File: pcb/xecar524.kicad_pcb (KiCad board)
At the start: 2 copper layers, 63.8 x 88.9 mm, 40 parts, among them J1 JTAG, J2 PROG, J3 Conn_02x02_Odd_Even, U1 MCP1703A-3302_SOT89, U2 Atari_XE_Cartridge_Connector, U3 XC95144XL-TQ100, U4 SST39VF040

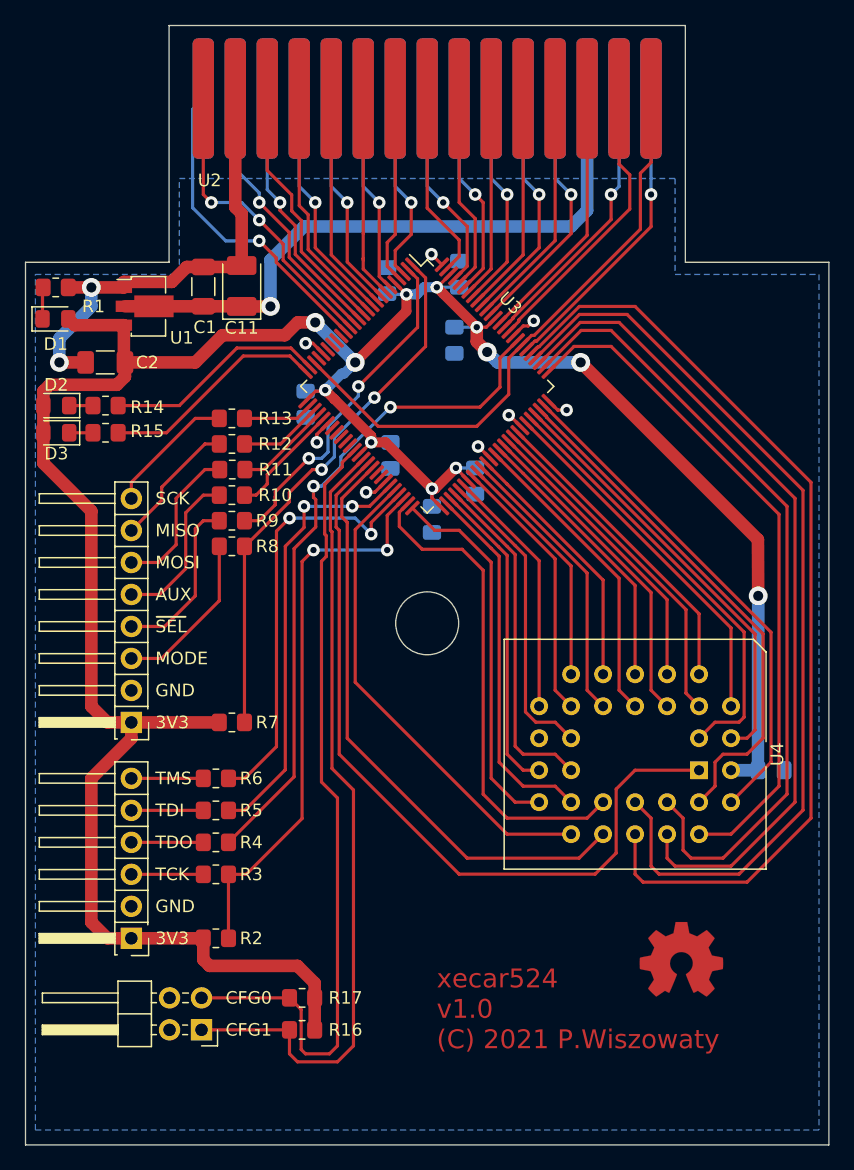
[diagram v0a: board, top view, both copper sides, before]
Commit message: PCB: Add top GND copper pour
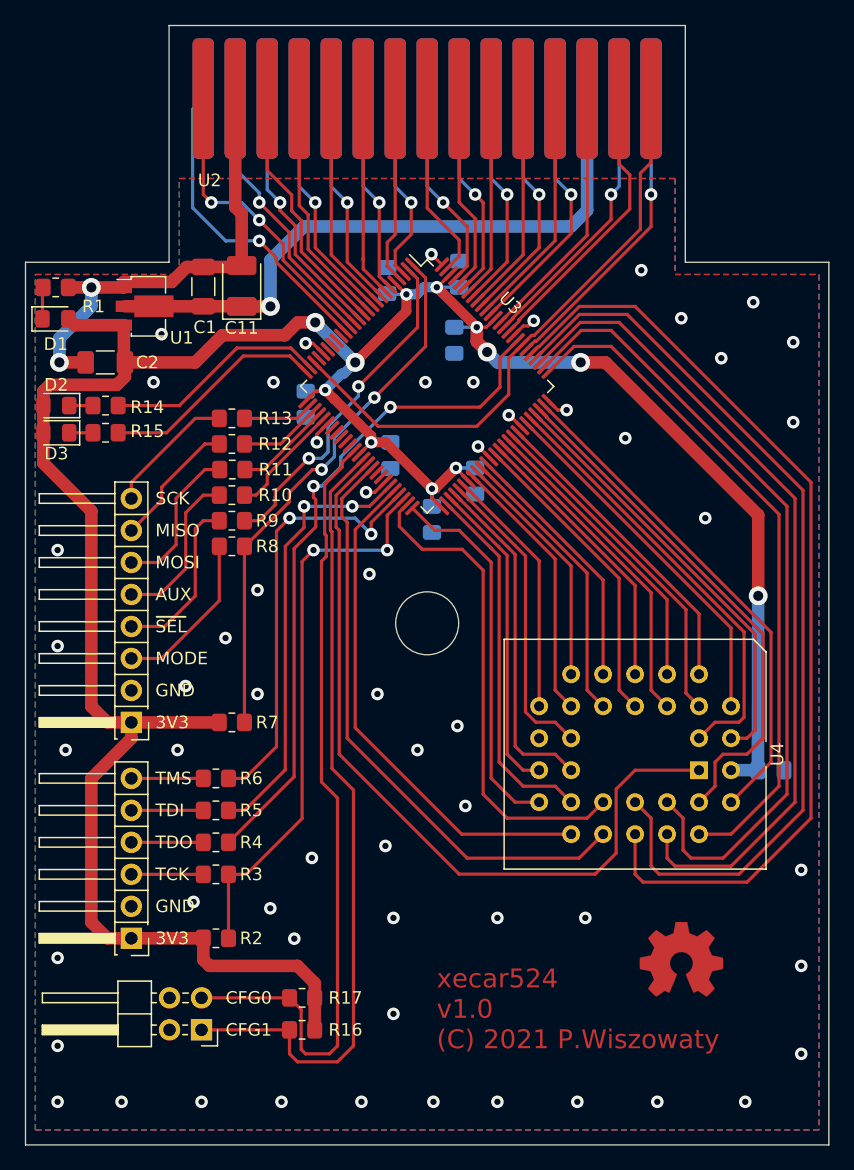
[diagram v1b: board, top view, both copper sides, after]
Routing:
- net ROM_D7: track 38.7 -> 40.8 mm
- net +3V3: track 220.6 -> 221.8 mm
- net GND: vias 10 -> 60
- added copper zone on F.Cu, net GND
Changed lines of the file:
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@@
     (thickness 1.6)
     (drawings 26)
-    (tracks 608)
+    (tracks 659)
     (zones 0)
     (modules 40)
@@
   (segment (start 135.268 59.644) (end 134.76 59.136) (width 1) (layer F.Cu) (net 3))
   (segment (start 135.268 63.76) (end 135.268 59.644) (width 1) (layer F.Cu) (net 3))
+  (via (at 139.446 117.221) (size 1) (drill 0.5) (layers F.Cu B.Cu) (net 3))
+  (via (at 137.541 114.808) (size 1) (drill 0.5) (layers F.Cu B.Cu) (net 3))
+  (via (at 140.843 110.8075) (size 1) (drill 0.5) (layers F.Cu B.Cu) (net 3))
+  (via (at 153.035 106.68) (size 1) (drill 0.5) (layers F.Cu B.Cu) (net 3))
+  (via (at 152.4 100.33) (size 1) (drill 0.5) (layers F.Cu B.Cu) (net 3))
+  (via (at 149.225 102.235) (size 1) (drill 0.5) (layers F.Cu B.Cu) (net 3))
+  (via (at 146.05 97.79) (size 1) (drill 0.5) (layers F.Cu B.Cu) (net 3))
+  (via (at 145.415 88.265) (size 1) (drill 0.5) (layers F.Cu B.Cu) (net 3))
+  (via (at 179.07 76.2) (size 1) (drill 0.5) (layers F.Cu B.Cu) (net 3))
+  (via (at 179.07 69.85) (size 1) (drill 0.5) (layers F.Cu B.Cu) (net 3))
+  (via (at 175.895 66.675) (size 1) (drill 0.5) (layers F.Cu B.Cu) (net 3))
+  (via (at 173.355 71.12) (size 1) (drill 0.5) (layers F.Cu B.Cu) (net 3))
+  (via (at 170.18 67.945) (size 1) (drill 0.5) (layers F.Cu B.Cu) (net 3))
+  (via (at 167.005 64.135) (size 1) (drill 0.5) (layers F.Cu B.Cu) (net 3))
+  (via (at 149.86 73.025) (size 1) (drill 0.5) (layers F.Cu B.Cu) (net 3))
+  (via (at 153.67 73.025) (size 1) (drill 0.5) (layers F.Cu B.Cu) (net 3))
+  (via (at 137.795 73.025) (size 1) (drill 0.5) (layers F.Cu B.Cu) (net 3))
+  (via (at 128.27 73.025) (size 1) (drill 0.5) (layers F.Cu B.Cu) (net 3))
+  (via (at 128.905 69.215) (size 1) (drill 0.5) (layers F.Cu B.Cu) (net 3))
+  (via (at 130.175 102.235) (size 1) (drill 0.5) (layers F.Cu B.Cu) (net 3))
+  (via (at 136.525 97.79) (size 1) (drill 0.5) (layers F.Cu B.Cu) (net 3))
+  (via (at 136.525 89.535) (size 1) (drill 0.5) (layers F.Cu B.Cu) (net 3))
+  (via (at 165.735 77.47) (size 1) (drill 0.5) (layers F.Cu B.Cu) (net 3))
+  (via (at 172.085 83.82) (size 1) (drill 0.5) (layers F.Cu B.Cu) (net 3))
+  (via (at 120.65 86.36) (size 1) (drill 0.5) (layers F.Cu B.Cu) (net 3))
+  (via (at 120.65 93.98) (size 1) (drill 0.5) (layers F.Cu B.Cu) (net 3))
+  (via (at 130.81 97.155) (size 1) (drill 0.5) (layers F.Cu B.Cu) (net 3))
+  (via (at 133.985 93.345) (size 1) (drill 0.5) (layers F.Cu B.Cu) (net 3))
+  (via (at 121.285 102.235) (size 1) (drill 0.5) (layers F.Cu B.Cu) (net 3))
+  (via (at 131.445 114.3) (size 1) (drill 0.5) (layers F.Cu B.Cu) (net 3))
+  (via (at 120.65 118.745) (size 1) (drill 0.5) (layers F.Cu B.Cu) (net 3))
+  (via (at 120.65 125.73) (size 1) (drill 0.5) (layers F.Cu B.Cu) (net 3))
+  (via (at 120.65 130.175) (size 1) (drill 0.5) (layers F.Cu B.Cu) (net 3))
+  (via (at 125.73 130.175) (size 1) (drill 0.5) (layers F.Cu B.Cu) (net 3))
+  (via (at 132.08 130.175) (size 1) (drill 0.5) (layers F.Cu B.Cu) (net 3))
+  (via (at 138.43 130.175) (size 1) (drill 0.5) (layers F.Cu B.Cu) (net 3))
+  (via (at 144.78 130.175) (size 1) (drill 0.5) (layers F.Cu B.Cu) (net 3))
+  (via (at 150.495 130.175) (size 1) (drill 0.5) (layers F.Cu B.Cu) (net 3))
+  (via (at 155.575 130.175) (size 1) (drill 0.5) (layers F.Cu B.Cu) (net 3))
+  (via (at 161.925 130.175) (size 1) (drill 0.5) (layers F.Cu B.Cu) (net 3))
+  (via (at 168.275 130.175) (size 1) (drill 0.5) (layers F.Cu B.Cu) (net 3))
+  (via (at 175.26 130.175) (size 1) (drill 0.5) (layers F.Cu B.Cu) (net 3))
+  (via (at 179.705 126.365) (size 1) (drill 0.5) (layers F.Cu B.Cu) (net 3))
+  (via (at 179.705 119.38) (size 1) (drill 0.5) (layers F.Cu B.Cu) (net 3))
+  (via (at 179.705 111.76) (size 1) (drill 0.5) (layers F.Cu B.Cu) (net 3))
+  (via (at 162.56 115.57) (size 1) (drill 0.5) (layers F.Cu B.Cu) (net 3))
+  (via (at 155.575 115.57) (size 1) (drill 0.5) (layers F.Cu B.Cu) (net 3))
+  (via (at 147.32 115.57) (size 1) (drill 0.5) (layers F.Cu B.Cu) (net 3))
+  (via (at 147.32 123.19) (size 1) (drill 0.5) (layers F.Cu B.Cu) (net 3))
+  (via (at 146.685 109.855) (size 1) (drill 0.5) (layers F.Cu B.Cu) (net 3))
   (segment (start 122 68.5) (end 121.5 68) (width 1) (layer F.Cu) (net 4))
   (segment (start 125.9125 68.5) (end 122 68.5) (width 1) (layer F.Cu) (net 4))
@@
   (segment (start 150.381 81.488) (end 150.635 81.488) (width 0.8) (layer F.Cu) (net 4))
   (via (at 162.192 71.455) (size 1.5) (drill 0.8) (layers F.Cu B.Cu) (net 4))
-  (segment (start 176.2675 85.5305) (end 162.192 71.455) (width 1) (layer F.Cu) (net 4))
-  (segment (start 176.289 89.997) (end 176.2675 85.5305) (width 1) (layer F.Cu) (net 4))
   (segment (start 176.2675 103.84) (end 176.289 89.997) (width 1) (layer B.Cu) (net 4))
   (via (at 176.289 89.997) (size 1.5) (drill 0.8) (layers F.Cu B.Cu) (net 4))
@@
   (segment (start 139.7 119.38) (end 141.065 120.745) (width 1) (layer F.Cu) (net 4))
   (segment (start 141.065 121.92) (end 141.065 124.46) (width 1) (layer F.Cu) (net 4))
+  (segment (start 162.192 71.455) (end 164.165 71.455) (width 1) (layer F.Cu) (net 4))
+  (segment (start 176.289 83.579) (end 176.289 89.997) (width 1) (layer F.Cu) (net 4))
+  (segment (start 164.165 71.455) (end 176.289 83.579) (width 1) (layer F.Cu) (net 4))
   (segment (start 134.22 117.19) (end 134.22 112.11) (width 0.254) (layer F.Cu) (net 5))
   (segment (start 146.825 86.36) (end 146.825 83.606068) (width 0.254) (layer F.Cu) (net 5))
@@
   (segment (start 158.89 87.199747) (end 152.943332 81.253079) (width 0.254) (layer F.Cu) (net 57))
   (segment (start 158.89 98.76) (end 158.89 87.199747) (width 0.254) (layer F.Cu) (net 57))
-  (segment (start 156.35 108.92) (end 161.43 108.92) (width 0.254) (layer F.Cu) (net 58))
-  (segment (start 144.285 96.855) (end 156.35 108.92) (width 0.254) (layer F.Cu) (net 58))
-  (segment (start 144.285 84.731856) (end 144.285 96.855) (width 0.254) (layer F.Cu) (net 58))
-  (segment (start 147.410221 81.606633) (end 144.285 84.731856) (width 0.254) (layer F.Cu) (net 58))
+  (segment (start 144.285 84.731856) (end 147.410221 81.606633) (width 0.254) (layer F.Cu) (net 58))
+  (segment (start 144.285 100.47) (end 144.285 84.731856) (width 0.254) (layer F.Cu) (net 58))
+  (segment (start 152.735 108.92) (end 144.285 100.47) (width 0.254) (layer F.Cu) (net 58))
+  (segment (start 161.43 108.92) (end 152.735 108.92) (width 0.254) (layer F.Cu) (net 58))
   (segment (start 160.16 102.57) (end 161.43 103.84) (width 0.254) (layer F.Cu) (net 59))
   (segment (start 157.62 102.57) (end 160.16 102.57) (width 0.254) (layer F.Cu) (net 59))
@@
     (connect_pads (clearance 0.508))
     (min_thickness 0.254)
+    (fill yes (arc_segments 32) (thermal_gap 0.508) (thermal_bridge_width 0.508) (smoothing fillet) (radius 0.4))
+    (polygon
+      (pts
+        (xy 169.685 64.47) (xy 181.115 64.47) (xy 181.115 132.415) (xy 118.885 132.415) (xy 118.885 64.47)
+        (xy 130.315 64.47) (xy 130.315 56.85) (xy 169.685 56.85)
+      )
+    )
+  )
+  (zone (net 3) (net_name GND) (layer F.Cu) (hatch edge 0.508)
+    (connect_pads (clearance 0.508))
+    (min_thickness 0.254)

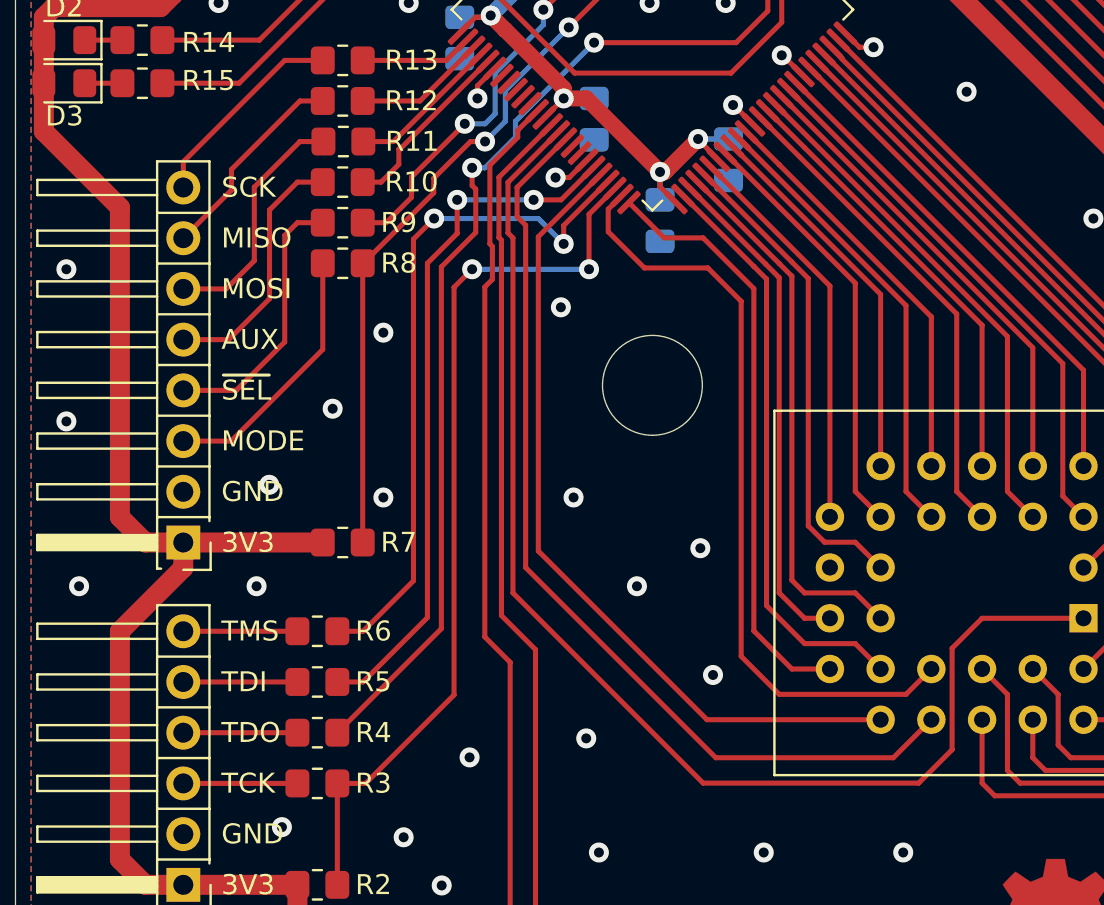
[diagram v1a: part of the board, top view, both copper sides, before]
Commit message: PCB: Tweak some tracks
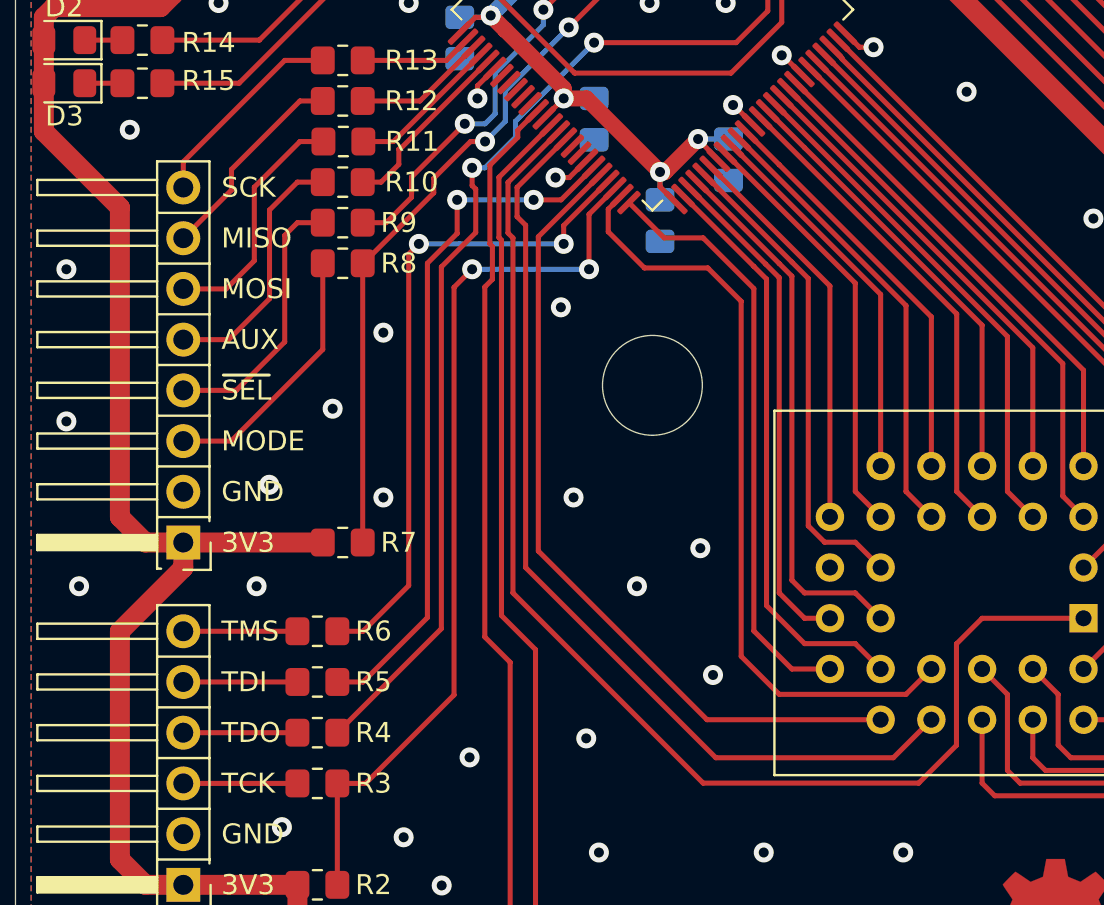
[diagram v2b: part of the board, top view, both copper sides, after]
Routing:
- net TMS: track 34.5 -> 33.1 mm
- net GND: vias 60 -> 61
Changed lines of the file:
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@@
     (thickness 1.6)
     (drawings 26)
-    (tracks 659)
+    (tracks 660)
     (zones 0)
     (modules 40)
@@
   (via (at 147.32 123.19) (size 1) (drill 0.5) (layers F.Cu B.Cu) (net 3))
   (via (at 146.685 109.855) (size 1) (drill 0.5) (layers F.Cu B.Cu) (net 3))
+  (via (at 123.825 79.375) (size 1) (drill 0.5) (layers F.Cu B.Cu) (net 3))
   (segment (start 122 68.5) (end 121.5 68) (width 1) (layer F.Cu) (net 4))
   (segment (start 125.9125 68.5) (end 122 68.5) (width 1) (layer F.Cu) (net 4))
@@
   (segment (start 145.555 85.09) (end 145.555 84.168961) (width 0.254) (layer F.Cu) (net 8))
   (via (at 145.555 85.09) (size 1) (drill 0.5) (layers F.Cu B.Cu) (net 8))
-  (via (at 139.065 83.82) (size 1) (drill 0.5) (layers F.Cu B.Cu) (net 8))
   (segment (start 135.507 104.49) (end 134.22 104.49) (width 0.254) (layer F.Cu) (net 8))
-  (segment (start 138.0325 101.9645) (end 135.507 104.49) (width 0.254) (layer F.Cu) (net 8))
-  (segment (start 138.0325 84.8525) (end 138.0325 101.9645) (width 0.254) (layer F.Cu) (net 8))
-  (segment (start 139.065 83.82) (end 138.0325 84.8525) (width 0.254) (layer F.Cu) (net 8))
-  (segment (start 144.285 83.82) (end 145.555 85.09) (width 0.254) (layer B.Cu) (net 8))
-  (segment (start 139.065 83.82) (end 144.285 83.82) (width 0.254) (layer B.Cu) (net 8))
+  (segment (start 140.335 85.09) (end 145.555 85.09) (width 0.254) (layer B.Cu) (net 8))
+  (segment (start 138.303 85.09) (end 140.335 85.09) (width 0.254) (layer B.Cu) (net 8))
+  (via (at 138.303 85.09) (size 1) (drill 0.5) (layers F.Cu B.Cu) (net 8))
+  (segment (start 138.303 85.09) (end 137.795 85.598) (width 0.254) (layer F.Cu) (net 8))
+  (segment (start 137.795 102.202) (end 135.507 104.49) (width 0.254) (layer F.Cu) (net 8))
+  (segment (start 137.795 85.598) (end 137.795 102.202) (width 0.254) (layer F.Cu) (net 8))
   (segment (start 131.37 51.35) (end 132.22 50.5) (width 0.254) (layer B.Cu) (net 9))
   (segment (start 131.37 59.175) (end 131.37 51.35) (width 0.254) (layer B.Cu) (net 9))
@@
   (segment (start 137.3 81.107) (end 137.3 80.345) (width 0.254) (layer F.Cu) (net 90))
   (segment (start 137.935 75.9) (end 135.49 75.9) (width 0.254) (layer F.Cu) (net 91))
-  (segment (start 142.767022 84.542022) (end 143.015 84.79) (width 0.254) (layer F.Cu) (net 92))
-  (segment (start 163.335 112.095) (end 165.008201 110.421799) (width 0.254) (layer F.Cu) (net 92))
-  (segment (start 165.008201 110.421799) (end 165.008201 105.341799) (width 0.254) (layer F.Cu) (net 92))
   (segment (start 166.51 103.84) (end 171.59 103.84) (width 0.254) (layer F.Cu) (net 92))
-  (segment (start 165.008201 105.341799) (end 166.51 103.84) (width 0.254) (layer F.Cu) (net 92))
-  (segment (start 145.288901 79.485312) (end 142.767022 82.007191) (width 0.254) (layer F.Cu) (net 92))
-  (segment (start 143.015 102.57) (end 152.54 112.095) (width 0.254) (layer F.Cu) (net 92))
+  (segment (start 165.227 105.123) (end 166.51 103.84) (width 0.254) (layer F.Cu) (net 92))
   (segment (start 152.54 112.095) (end 163.335 112.095) (width 0.254) (layer F.Cu) (net 92))
-  (segment (start 142.767022 82.007191) (end 142.767022 84.542022) (width 0.254) (layer F.Cu) (net 92))
+  (segment (start 165.227 110.203) (end 165.227 105.123) (width 0.254) (layer F.Cu) (net 92))
+  (segment (start 143.015 102.57) (end 152.54 112.095) (width 0.254) (layer F.Cu) (net 92))
+  (segment (start 163.335 112.095) (end 165.227 110.203) (width 0.254) (layer F.Cu) (net 92))
   (segment (start 143.015 84.79) (end 143.015 102.57) (width 0.254) (layer F.Cu) (net 92))
+  (segment (start 142.767022 84.542022) (end 143.015 84.79) (width 0.254) (layer F.Cu) (net 92))
+  (segment (start 142.767022 82.007191) (end 142.767022 84.542022) (width 0.254) (layer F.Cu) (net 92))
+  (segment (start 145.288901 79.485312) (end 142.767022 82.007191) (width 0.254) (layer F.Cu) (net 92))
   (segment (start 121.57 74.884) (end 123.457 74.884) (width 0.254) (layer F.Cu) (net 95))
   (segment (start 121.57 77.043) (end 123.457 77.043) (width 0.254) (layer F.Cu) (net 96))
@@
       )
     )
+  )
+  (zone (net 0) (net_name "") (layer F.Cu) (hatch edge 0.508)
+    (connect_pads (clearance 0.508))
+    (min_thickness 0.254)
+    (keepout (tracks allowed) (vias allowed) (copperpour not_allowed))
+    (fill (arc_segments 32) (thermal_gap 0.508) (thermal_bridge_width 0.508) (smoothing fillet) (radius 0.4))
+    (polygon
+      (pts
+        (xy 177.165 118.745) (xy 177.165 127) (xy 176.53 127.635) (xy 150.495 127.635) (xy 149.86 127)
+        (xy 149.86 118.745) (xy 150.495 118.11) (xy 163.83 118.11) (xy 167.005 114.935) (xy 173.355 114.935)
+      )
+    )
